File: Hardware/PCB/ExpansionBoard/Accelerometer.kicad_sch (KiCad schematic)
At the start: 3 parts, among them U201 ADXL372BCCZ-RL7

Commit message: INT BUS
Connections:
- net INT_1: now reaches U201.11 (INT1)
- net INT_2: now reaches U201.9 (INT2)
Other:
- note added: "Recommended Interrupt Pin Configuration for Velocity Tracking: Use the Data Ready Interrupt: Purpose: Trigger an interrupt each time new acceleration data is available. This ensures your system can collect data at the sensor's Output Data Rate (ODR). Action: Configure the DATA_READY interrupt and map it to one of the pins (INT1 or INT2). Reason: This minimizes latency and ensures synchronization 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"
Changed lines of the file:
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@@
 	(generator_version "8.0")
 	(paper "A4")
+	(bus_alias "INT"
+		(members "INT_1" "INT_2")
+	)
 	(bus_alias "SPI"
 		(members "SCLK" "MOSI" "MISO" "~{CS}")
@@
 	)
 	(bus_entry
+		(at 142.24 78.74)
+		(size -2.54 -2.54)
+		(stroke
+			(width 0)
+			(type default)
+		)
+	)
+	(bus_entry
+		(at 142.24 82.55)
+		(size -2.54 -2.54)
+		(stroke
+			(width 0)
+			(type default)
+		)
+	)
+	(bus_entry
 		(at 93.98 71.12)
 		(size 2.54 2.54)
@@
 		)
 	)
+	(wire
+		(pts
+			(xy 134.62 80.01) (xy 139.7 80.01)
+		)
+		(stroke
+			(width 0)
+			(type default)
+		)
+	)
+	(bus
+		(pts
+			(xy 142.24 74.93) (xy 142.24 78.74)
+		)
+		(stroke
+			(width 0)
+			(type default)
+		)
+	)
 	(bus
 		(pts
@@
 		)
 	)
+	(bus
+		(pts
+			(xy 142.24 78.74) (xy 142.24 82.55)
+		)
+		(stroke
+			(width 0)
+			(type default)
+		)
+	)
 	(wire
 		(pts
@@
 	(wire
 		(pts
+			(xy 139.7 76.2) (xy 134.62 76.2)
+		)
+		(stroke
+			(width 0)
+			(type default)
+		)
+	)
+	(wire
+		(pts
 			(xy 123.19 55.88) (xy 113.03 55.88)
 		)
@@
 		)
 	)
+	(bus
+		(pts
+			(xy 142.24 82.55) (xy 142.24 83.82)
+		)
+		(stroke
+			(width 0)
+			(type default)
+		)
+	)
+	(bus
+		(pts
+			(xy 142.24 83.82) (xy 153.67 83.82)
+		)
+		(stroke
+			(width 0)
+			(type default)
+		)
+	)
 	(wire
 		(pts
@@
 			(width 0)
 			(type default)
+		)
+	)
+	(text "Recommended Interrupt Pin Configuration for Velocity Tracking:\nUse the Data Ready Interrupt:\n\nPurpose: Trigger an interrupt each time new acceleration data is available. This ensures your system can collect data at the sensor's Output Data Rate (ODR).\nAction: Configure the DATA_READY interrupt and map it to one of the pins (INT1 or INT2).\nReason: This minimizes latency and ensures synchronization between the sensor and your microcontroller for real-time velocity computation.\n\n\n\nOptional: Use FIFO Watermark Interrupt:\n\nPurpose: If you want to reduce the number of interactions with the sensor, you can use the FIFO. Configure a watermark interrupt to trigger when the FIFO is partially full (e.g., every 64 samples).\nAction: Map the FIFO_WATERMARK interrupt to the second interrupt pin (INT2).\nReason: This approach helps reduce the burden on your microcontroller, which can process data in batches instead of continuously reading acceleration values."
+		(exclude_from_sim no)
+		(at 13.716 28.956 0)
+		(effects
+			(font
+				(size 1.27 1.27)
+			)
+			(justify left)
 		)
 	)
@@
 	(label "MOSI"
 		(at 96.52 76.2 0)
+		(fields_autoplaced yes)
+		(effects
+			(font
+				(size 1.27 1.27)
+			)
+			(justify left bottom)
+		)
+	)
+	(label "{INT}"
+		(at 142.24 74.93 0)
+		(fields_autoplaced yes)
+		(effects
+			(font
+				(size 1.27 1.27)
+			)
+			(justify left bottom)
+		)
+	)
+	(label "INT_2"
+		(at 134.62 80.01 0)
+		(effects
+			(font
+				(size 1.27 1.27)
+			)
+			(justify left bottom)
+		)
+	)
+	(label "INT_1"
+		(at 134.62 76.2 0)
 		(effects
 			(font
@@
 	(label "~{CS}"
 		(at 96.52 81.28 0)
+		(fields_autoplaced yes)
 		(effects
 			(font
@@
 	(label "MISO"
 		(at 96.52 78.74 0)
+		(fields_autoplaced yes)
 		(effects
 			(font
@@
 	(label "SCLK"
 		(at 96.52 73.66 0)
-		(effects
-			(font
-				(size 1.27 1.27)
-			)
-			(justify left bottom)
-		)
-	)
+		(fields_autoplaced yes)
+		(effects
+			(font
+				(size 1.27 1.27)
+			)
+			(justify left bottom)
+		)
+	)
+	(hierarchical_label "INT"
+		(shape output)
+		(at 153.67 83.82 0)
+		(fields_autoplaced yes)
+		(effects
+			(font
+				(size 1.27 1.27)
+			)
+			(justify left)
+		)
+	)

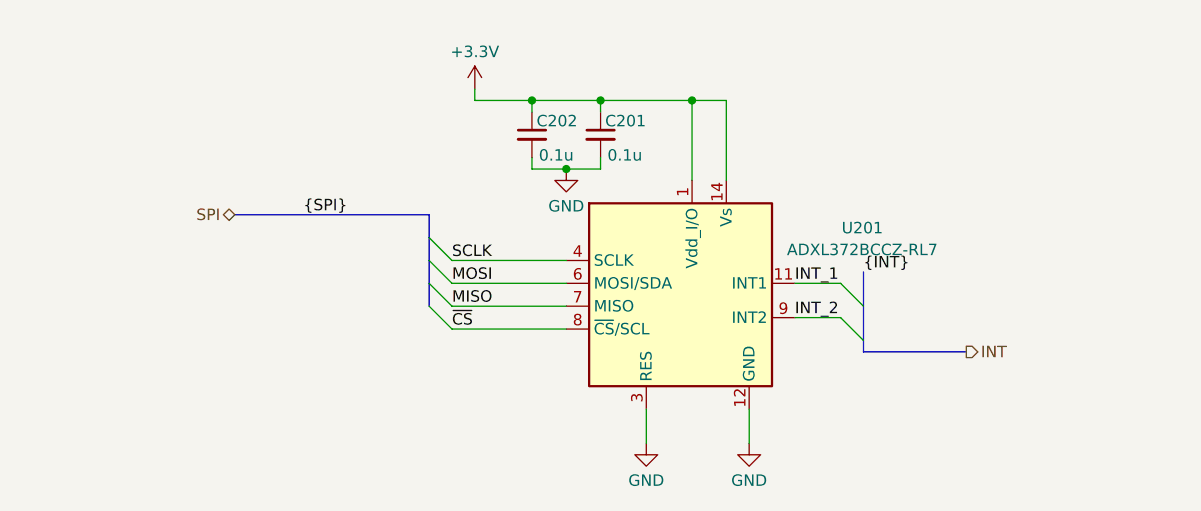
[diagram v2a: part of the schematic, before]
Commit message: DONE: PWR LED MISSING AND AIRSPEED
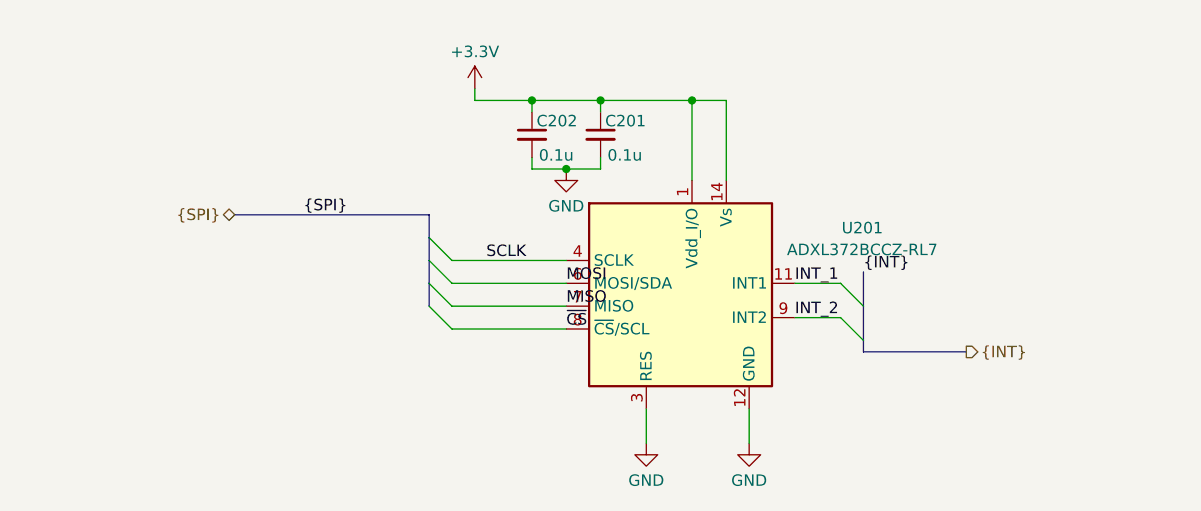
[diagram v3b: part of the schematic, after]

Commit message: finished schema
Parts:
- C201, C202: footprint (none) -> Capacitor_SMD:C_0805_2012Metric_Pad1.18x1.45mm_HandSolder
- U201: footprint (none) -> DynamicSoaring:ADXL372BCCZ-RL7
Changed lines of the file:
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@@
 	)
 	(label "MOSI"
-		(at 109.22 76.2 0)
+		(at 100.33 76.2 0)
 		(fields_autoplaced yes)
 		(effects
@@
 	)
 	(label "MISO"
-		(at 109.22 78.74 0)
+		(at 100.33 78.74 0)
 		(fields_autoplaced yes)
 		(effects
@@
 	)
 	(label "~{CS}"
-		(at 109.22 81.28 0)
+		(at 100.33 81.28 0)
 		(fields_autoplaced yes)
 		(effects
@@
 			)
 		)
-		(property "Footprint" ""
+		(property "Footprint" "DynamicSoaring:ADXL372BCCZ-RL7"
 			(at 91.694 59.182 0)
 			(effects
@@
 			)
 		)
-		(property "Footprint" ""
+		(property "Footprint" "Capacitor_SMD:C_0805_2012Metric_Pad1.18x1.45mm_HandSolder"
 			(at 105.41 59.69 0)
 			(effects
@@
 			)
 		)
-		(property "Footprint" ""
+		(property "Footprint" "Capacitor_SMD:C_0805_2012Metric_Pad1.18x1.45mm_HandSolder"
 			(at 113.03 59.69 0)
 			(effects

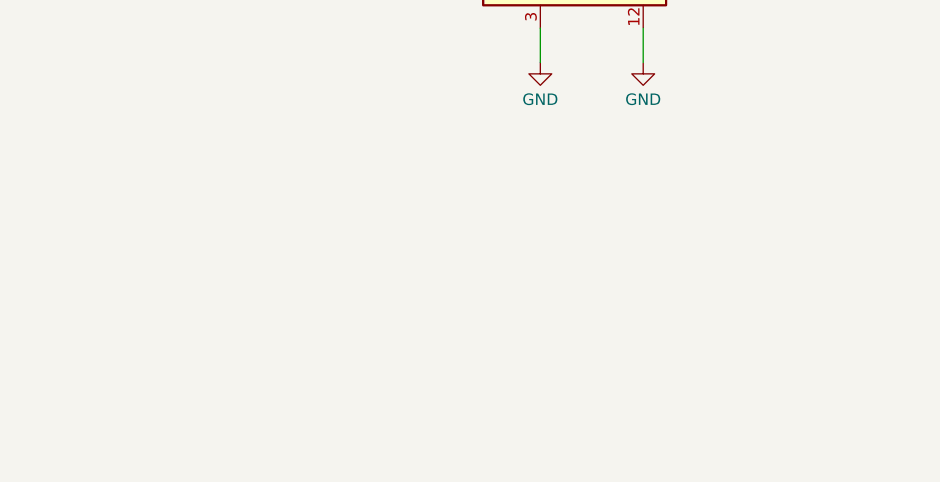
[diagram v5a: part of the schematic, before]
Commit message: added Cube Project, SD Card and Tillt Switch
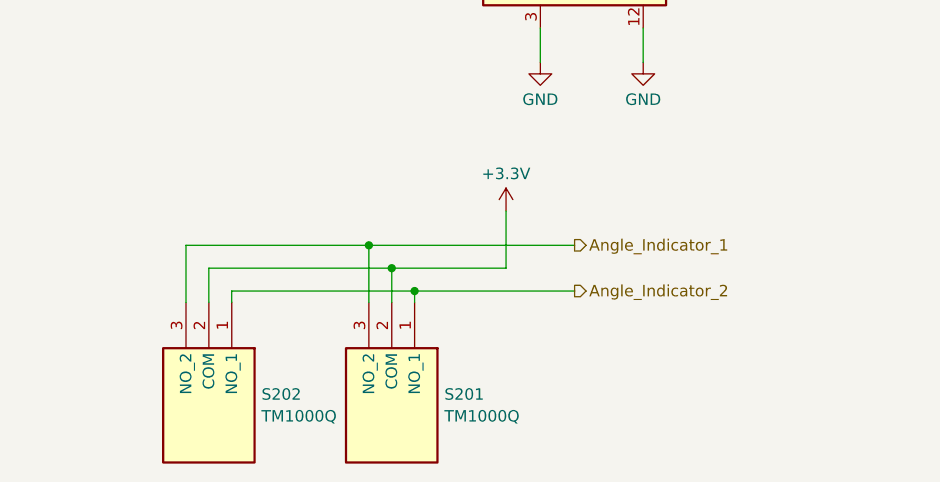
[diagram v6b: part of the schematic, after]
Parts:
- added S201, S202: TM1000Q, SamacSys_Parts:TM1000Q, symbol SamacSys_Parts:TM1000Q
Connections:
- net +3.3V: now also S201.2 (COM), S202.2 (COM)
- new net Angle_Indicator_1: S201.3 (NO_2), S202.3 (NO_2)
- new net Angle_Indicator_2: S201.1 (NO_1), S202.1 (NO_1)

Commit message: finished pcb layout
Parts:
- S201, S202: footprint SamacSys_Parts:TM1000Q -> TM1000Q
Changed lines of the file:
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@@
 			)
 		)
-		(property "Footprint" "SamacSys_Parts:TM1000Q"
+		(property "Footprint" "TM1000Q"
 			(at 9.22 139.7 0)
 			(effects
@@
 			)
 		)
-		(property "Footprint" "SamacSys_Parts:TM1000Q"
+		(property "Footprint" "TM1000Q"
 			(at -11.1 139.7 0)
 			(effects

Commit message: finsihed pcb
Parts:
- S201, S202: footprint TM1000Q -> SamacSys_Parts:TM1000Q
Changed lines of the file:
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@@
 			)
 		)
-		(property "Footprint" "TM1000Q"
+		(property "Footprint" "SamacSys_Parts:TM1000Q"
 			(at 9.22 139.7 0)
 			(effects
@@
 			)
 		)
-		(property "Footprint" "TM1000Q"
+		(property "Footprint" "SamacSys_Parts:TM1000Q"
 			(at -11.1 139.7 0)
 			(effects
